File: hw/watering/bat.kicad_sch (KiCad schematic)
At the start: 13 parts, among them U5 STI3508

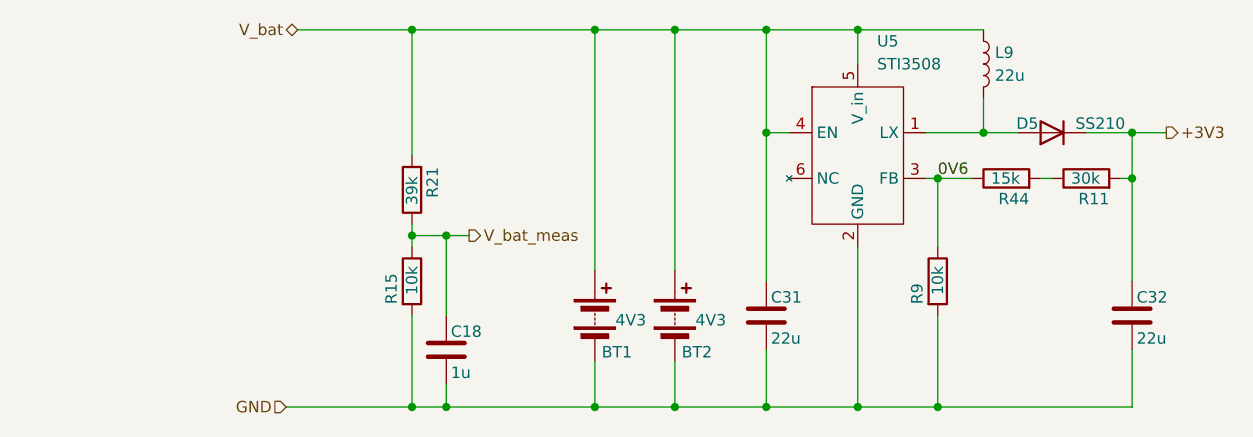
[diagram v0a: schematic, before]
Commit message: - hw   - rewired power input for battery   - some first placing of parts on pcb but no routing - sw   - added example http server from examples to server.cpp, not compilable yet
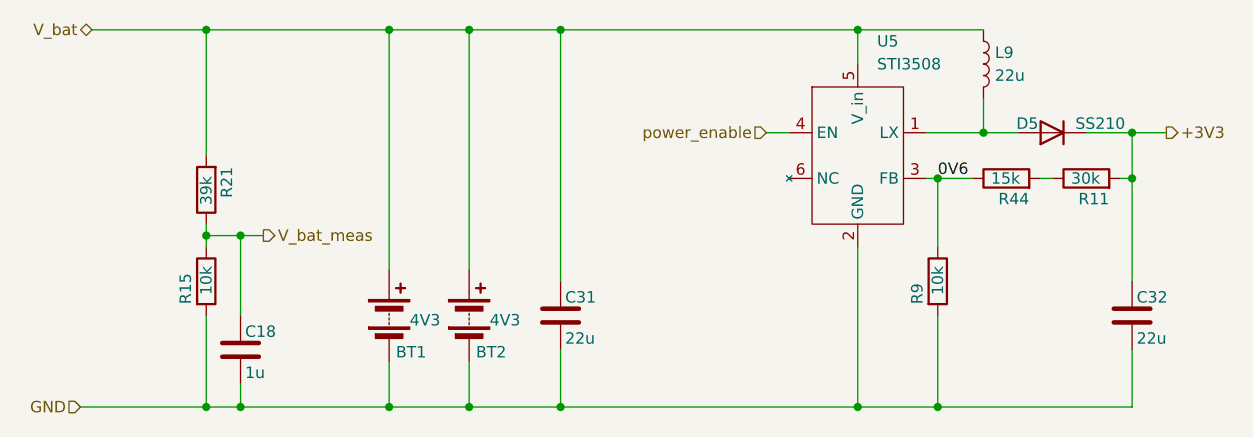
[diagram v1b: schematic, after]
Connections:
- net V_bat: no longer U5.4 (EN)
- new net power_enable: U5.4 (EN)
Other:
- moved on the sheet: BT1, BT2, C18, C31, R15, R21
